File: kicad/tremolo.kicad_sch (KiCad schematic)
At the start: 20 parts, among them IC2 TL072CP

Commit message: Datasheet footprints, floor-plan placement, headless autoroute (144/145, DRC 0)
PCB-AUDIT s1 fixes with datasheet-derived project footprints:
- TO-220-5_Vertical_P1.70mm_LM1875 (TI NDH0005D): 1.45 mm pads on the 1.1 mm
  drill -> 0.175 mm annular (was 0.0875, 5 DRC errors); pad-local 0.2 mm clearance
- Bridge_KBP_P3.81mm (Diodes DS39310 KBP404G-KBP410G, pins + ~ ~ -); bridge
  symbol renumbered to the physical order; errata #3 updated (KBU needs a swap)
- value-aware CP/R sizing (real can sizes for 4700/2200/1000 uF, 5 W / 1 W
  resistors, fat pads on the 0R speaker return); Part 4 wire pads for all
  off-board wiring (2.0 mm/1.2 mm signal, 3.0 mm/1.5 mm speaker + transformer)
- VRAW/AC1/AC2 moved into the HighCurrent net class (errata #11)

gen_pcb.py now places to the Part 5 floor plan: balanced columns (Input/Preamp
with Tone stacked below | Reverb/Trem/MRB | Power Amp | PSU), signal order inside
zones with serpentine shelves, LM1875/LM317 on the top edge with the 10 mm
keep-out, wiring edge along the bottom, 4x M3 holes, two locked 0.9 mm escape
stubs off the LM1875 pins 4/5 (a 1.5/2.5 mm trace cannot enter a 1.70 mm pitch).
DRC before routing: 0 errors, 0 warnings.

route_board.py: pcbnew DSN export -> Freerouting -> SES import -> pour refill.
Freerouting 2.1.0 ignores every pass/timeout limit in CLI mode and only writes
output at 0 unrouted (and its MT router crashed), so the script drives 1.9.0
under xvfb-run and injects autoroute_settings (bottom layer 6x cost, via 80) so
the GND pour stays whole. Committed board: 144/145 connections routed, 0 DRC
violations (--severity-all), 26 vias, 351 mm on the bottom vs 3.7 m on top; the
one open PA_OUT link (blocked by R_bias1) is documented as a GUI finish.

Chassis-fit figure corrected: the old 48-53 % / 82-90 % densities counted hidden
text boxes; text-less it is ~33 % on 190x115 and ~56 % on 155x90.

Docs: PCB-NOTES/PCB-AUDIT rewritten, README, CHANGELOG, errata #3/#11,
SOURCES (package drawings), Part 10, kicad RE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
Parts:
- C_dc_blk: footprint Capacitor_THT:CP_Radial_D8.0mm_P3.50mm -> Capacitor_THT:CP_Radial_D5.0mm_P2.00mm
- POT_DPT, POT_SPD: footprint Connector_PinHeader_2.54mm:PinHeader_1x03_P2.54mm_Vertical -> cambridge_reverb:WirePad_1x03_P2.54mm_D1.2mm
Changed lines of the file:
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@@
     (pin "8")
     (pin "4")
-    (instances (project "cambridge_reverb" (path "/d42230cc-952b-4e7b-8b81-b7cfcd0de5be" (reference "IC2") (unit 1))))
+    (instances (project "cambridge_reverb" (path "/22b2c6fc-b800-4b3c-8b0c-9c9dd16d6c3e" (reference "IC2") (unit 1))))
   )
   (wire (pts (xy 191.76999999999998 116.84) (xy 189.23 116.84)) (stroke (width 0) (type default)))
@@
     (pin "1")
     (pin "2")
-    (instances (project "cambridge_reverb" (path "/d42230cc-952b-4e7b-8b81-b7cfcd0de5be" (reference "C_obuf_in") (unit 1))))
+    (instances (project "cambridge_reverb" (path "/22b2c6fc-b800-4b3c-8b0c-9c9dd16d6c3e" (reference "C_obuf_in") (unit 1))))
   )
   (wire (pts (xy 119.38 71.12) (xy 116.84 71.12)) (stroke (width 0) (type default)))
@@
     (pin "1")
     (pin "2")
-    (instances (project "cambridge_reverb" (path "/d42230cc-952b-4e7b-8b81-b7cfcd0de5be" (reference "R_obuf_b") (unit 1))))
+    (instances (project "cambridge_reverb" (path "/22b2c6fc-b800-4b3c-8b0c-9c9dd16d6c3e" (reference "R_obuf_b") (unit 1))))
   )
   (wire (pts (xy 119.38 101.6) (xy 116.84 101.6)) (stroke (width 0) (type default)))
@@
     (pin "1")
     (pin "2")
-    (instances (project "cambridge_reverb" (path "/d42230cc-952b-4e7b-8b81-b7cfcd0de5be" (reference "R_lfo_ser") (unit 1))))
+    (instances (project "cambridge_reverb" (path "/22b2c6fc-b800-4b3c-8b0c-9c9dd16d6c3e" (reference "R_lfo_ser") (unit 1))))
   )
   (wire (pts (xy 228.59999999999997 86.36) (xy 226.06 86.36)) (stroke (width 0) (type default)))
@@
     (property "Reference" "POT_SPD" (at 266.70000000000005 78.74 0) (effects (font (size 1.27 1.27)) (justify left)))
     (property "Value" "500k lin" (at 266.70000000000005 81.28 0) (effects (font (size 1.27 1.27)) (justify left)))
-    (property "Footprint" "Connector_PinHeader_2.54mm:PinHeader_1x03_P2.54mm_Vertical" (at 264.16 86.36 0) (effects (font (size 1.27 1.27)) hide))
+    (property "Footprint" "cambridge_reverb:WirePad_1x03_P2.54mm_D1.2mm" (at 264.16 86.36 0) (effects (font (size 1.27 1.27)) hide))
     (pin "1")
     (pin "3")
     (pin "2")
-    (instances (project "cambridge_reverb" (path "/d42230cc-952b-4e7b-8b81-b7cfcd0de5be" (reference "POT_SPD") (unit 1))))
+    (instances (project "cambridge_reverb" (path "/22b2c6fc-b800-4b3c-8b0c-9c9dd16d6c3e" (reference "POT_SPD") (unit 1))))
   )
   (wire (pts (xy 259.08 86.36) (xy 256.54 86.36)) (stroke (width 0) (type default)))
@@
     (pin "1")
     (pin "2")
-    (instances (project "cambridge_reverb" (path "/d42230cc-952b-4e7b-8b81-b7cfcd0de5be" (reference "C_lfo1") (unit 1))))
+    (instances (project "cambridge_reverb" (path "/22b2c6fc-b800-4b3c-8b0c-9c9dd16d6c3e" (reference "C_lfo1") (unit 1))))
   )
   (wire (pts (xy 288.28999999999996 91.44) (xy 285.75 91.44)) (stroke (width 0) (type default)))
@@
     (pin "1")
     (pin "2")
-    (instances (project "cambridge_reverb" (path "/d42230cc-952b-4e7b-8b81-b7cfcd0de5be" (reference "R_lfo1") (unit 1))))
+    (instances (project "cambridge_reverb" (path "/22b2c6fc-b800-4b3c-8b0c-9c9dd16d6c3e" (reference "R_lfo1") (unit 1))))
   )
   (wire (pts (xy 238.76 151.13) (xy 236.22000000000003 151.13)) (stroke (width 0) (type default)))
@@
     (pin "1")
     (pin "2")
-    (instances (project "cambridge_reverb" (path "/d42230cc-952b-4e7b-8b81-b7cfcd0de5be" (reference "C_lfo2") (unit 1))))
+    (instances (project "cambridge_reverb" (path "/22b2c6fc-b800-4b3c-8b0c-9c9dd16d6c3e" (reference "C_lfo2") (unit 1))))
   )
   (wire (pts (xy 274.32 151.13) (xy 271.78 151.13)) (stroke (width 0) (type default)))
@@
     (pin "1")
     (pin "2")
-    (instances (project "cambridge_reverb" (path "/d42230cc-952b-4e7b-8b81-b7cfcd0de5be" (reference "R_lfo_fb1") (unit 1))))
+    (instances (project "cambridge_reverb" (path "/22b2c6fc-b800-4b3c-8b0c-9c9dd16d6c3e" (reference "R_lfo_fb1") (unit 1))))
   )
   (wire (pts (xy 158.75 101.6) (xy 156.21 101.6)) (stroke (width 0) (type default)))
@@
     (pin "1")
     (pin "2")
-    (instances (project "cambridge_reverb" (path "/d42230cc-952b-4e7b-8b81-b7cfcd0de5be" (reference "R_lfo_fb2") (unit 1))))
+    (instances (project "cambridge_reverb" (path "/22b2c6fc-b800-4b3c-8b0c-9c9dd16d6c3e" (reference "R_lfo_fb2") (unit 1))))
   )
   (wire (pts (xy 158.75 142.24) (xy 156.21 142.24)) (stroke (width 0) (type default)))
@@
     (pin "1")
     (pin "2")
-    (instances (project "cambridge_reverb" (path "/d42230cc-952b-4e7b-8b81-b7cfcd0de5be" (reference "D_lfo1") (unit 1))))
+    (instances (project "cambridge_reverb" (path "/22b2c6fc-b800-4b3c-8b0c-9c9dd16d6c3e" (reference "D_lfo1") (unit 1))))
   )
   (wire (pts (xy 128.27 101.6) (xy 125.73 101.6)) (stroke (width 0) (type default)))
@@
     (pin "1")
     (pin "2")
-    (instances (project "cambridge_reverb" (path "/d42230cc-952b-4e7b-8b81-b7cfcd0de5be" (reference "D_lfo2") (unit 1))))
+    (instances (project "cambridge_reverb" (path "/22b2c6fc-b800-4b3c-8b0c-9c9dd16d6c3e" (reference "D_lfo2") (unit 1))))
   )
   (wire (pts (xy 128.27 132.07999999999998) (xy 125.73 132.07999999999998)) (stroke (width 0) (type default)))
@@
     (property "Reference" "POT_DPT" (at 212.09 173.99 0) (effects (font (size 1.27 1.27)) (justify left)))
     (property "Value" "100k lin" (at 212.09 176.53 0) (effects (font (size 1.27 1.27)) (justify left)))
-    (property "Footprint" "Connector_PinHeader_2.54mm:PinHeader_1x03_P2.54mm_Vertical" (at 209.55 181.61 0) (effects (font (size 1.27 1.27)) hide))
+    (property "Footprint" "cambridge_reverb:WirePad_1x03_P2.54mm_D1.2mm" (at 209.55 181.61 0) (effects (font (size 1.27 1.27)) hide))
     (pin "1")
     (pin "3")
     (pin "2")
-    (instances (project "cambridge_reverb" (path "/d42230cc-952b-4e7b-8b81-b7cfcd0de5be" (reference "POT_DPT") (unit 1))))
+    (instances (project "cambridge_reverb" (path "/22b2c6fc-b800-4b3c-8b0c-9c9dd16d6c3e" (reference "POT_DPT") (unit 1))))
   )
   (wire (pts (xy 204.47 181.61) (xy 201.93 181.61)) (stroke (width 0) (type default)))
@@
     (pin "1")
     (pin "2")
-    (instances (project "cambridge_reverb" (path "/d42230cc-952b-4e7b-8b81-b7cfcd0de5be" (reference "R_led") (unit 1))))
+    (instances (project "cambridge_reverb" (path "/22b2c6fc-b800-4b3c-8b0c-9c9dd16d6c3e" (reference "R_led") (unit 1))))
   )
   (wire (pts (xy 243.83999999999997 181.61) (xy 241.3 181.61)) (stroke (width 0) (type default)))
@@
     (pin "3")
     (pin "4")
-    (instances (project "cambridge_reverb" (path "/d42230cc-952b-4e7b-8b81-b7cfcd0de5be" (reference "VTL1") (unit 1))))
+    (instances (project "cambridge_reverb" (path "/22b2c6fc-b800-4b3c-8b0c-9c9dd16d6c3e" (reference "VTL1") (unit 1))))
   )
   (wire (pts (xy 285.75 179.07000000000002) (xy 283.21 179.07000000000002)) (stroke (width 0) (type default)))
@@
     (pin "1")
     (pin "2")
-    (instances (project "cambridge_reverb" (path "/d42230cc-952b-4e7b-8b81-b7cfcd0de5be" (reference "R_led_diag") (unit 1))))
+    (instances (project "cambridge_reverb" (path "/22b2c6fc-b800-4b3c-8b0c-9c9dd16d6c3e" (reference "R_led_diag") (unit 1))))
   )
   (wire (pts (xy 238.76 212.09) (xy 236.22000000000003 212.09)) (stroke (width 0) (type default)))
@@
     (pin "1")
     (pin "2")
-    (instances (project "cambridge_reverb" (path "/d42230cc-952b-4e7b-8b81-b7cfcd0de5be" (reference "LED_rate") (unit 1))))
+    (instances (project "cambridge_reverb" (path "/22b2c6fc-b800-4b3c-8b0c-9c9dd16d6c3e" (reference "LED_rate") (unit 1))))
   )
   (wire (pts (xy 284.48 212.09) (xy 281.94 212.09)) (stroke (width 0) (type default)))
@@
     (pin "1")
     (pin "2")
-    (instances (project "cambridge_reverb" (path "/d42230cc-952b-4e7b-8b81-b7cfcd0de5be" (reference "R_trem1") (unit 1))))
+    (instances (project "cambridge_reverb" (path "/22b2c6fc-b800-4b3c-8b0c-9c9dd16d6c3e" (reference "R_trem1") (unit 1))))
   )
   (wire (pts (xy 148.59 181.61) (xy 146.05 181.61)) (stroke (width 0) (type default)))
@@
     (property "Reference" "C_dc_blk" (at 156.21 204.47 0) (effects (font (size 1.27 1.27)) (justify left)))
     (property "Value" "10uF" (at 156.21 207.01 0) (effects (font (size 1.27 1.27)) (justify left)))
-    (property "Footprint" "Capacitor_THT:CP_Radial_D8.0mm_P3.50mm" (at 153.67000000000002 212.09 0) (effects (font (size 1.27 1.27)) hide))
-    (pin "1")
-    (pin "2")
-    (instances (project "cambridge_reverb" (path "/d42230cc-952b-4e7b-8b81-b7cfcd0de5be" (reference "C_dc_blk") (unit 1))))
+    (property "Footprint" "Capacitor_THT:CP_Radial_D5.0mm_P2.00mm" (at 153.67000000000002 212.09 0) (effects (font (size 1.27 1.27)) hide))
+    (pin "1")
+    (pin "2")
+    (instances (project "cambridge_reverb" (path "/22b2c6fc-b800-4b3c-8b0c-9c9dd16d6c3e" (reference "C_dc_blk") (unit 1))))
   )
   (wire (pts (xy 148.59 212.09) (xy 146.05 212.09)) (stroke (width 0) (type default)))
@@
     (pin "1")
     (pin "2")
-    (instances (project "cambridge_reverb" (path "/d42230cc-952b-4e7b-8b81-b7cfcd0de5be" (reference "R_fs_trem") (unit 1))))
+    (instances (project "cambridge_reverb" (path "/22b2c6fc-b800-4b3c-8b0c-9c9dd16d6c3e" (reference "R_fs_trem") (unit 1))))
   )
   (wire (pts (xy 119.38 212.09) (xy 116.84 212.09)) (stroke (width 0) (type default)))

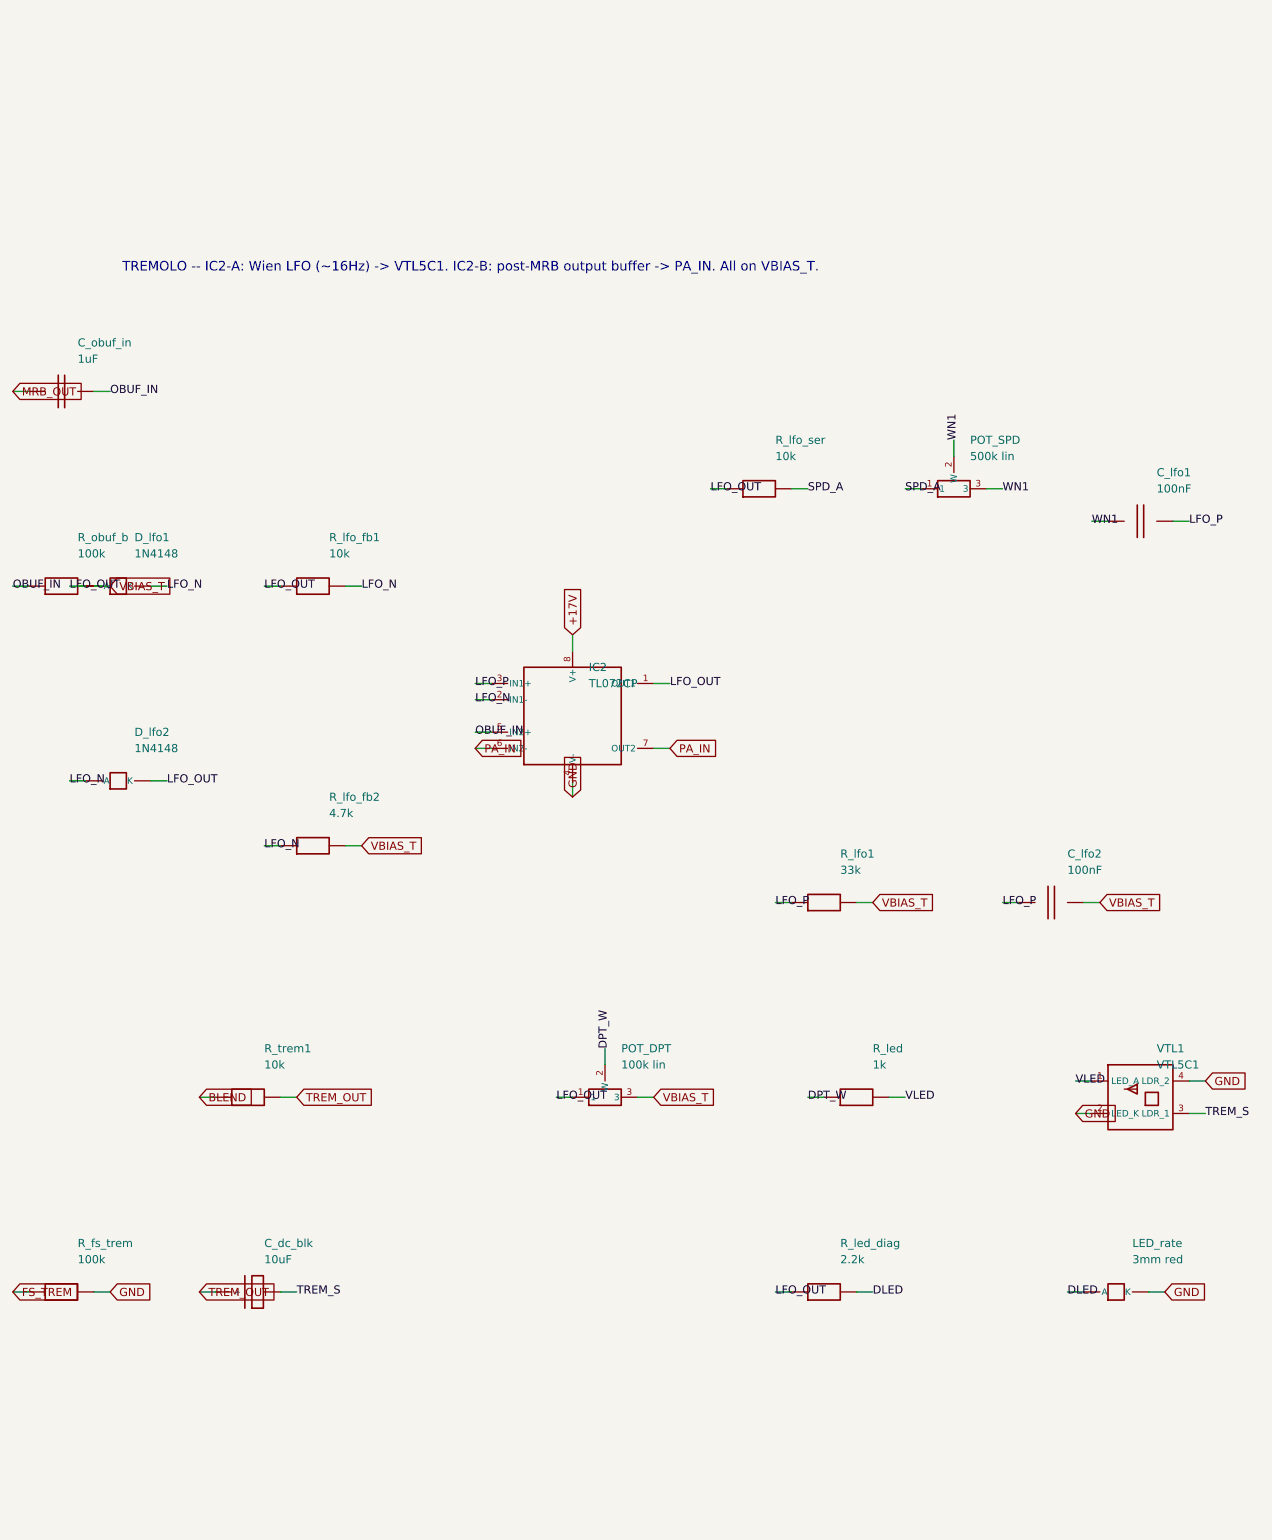
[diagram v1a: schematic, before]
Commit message: Add 26 labelled bench test points (schematic + BOM + silk) and re-route
Test points follow the Part 5 bring-up order: rails (VRAW, +33V5, VREG_IN,
+17V), JFET drains Q1D/Q2D/QRD (the errata #15 bias trim), the VBIAS_R/VBIAS_T
mid-rail refs, every inter-stage node (PREAMP_OUT, TONE_OUT, BLEND, TREM_OUT,
MRB_OUT, PA_IN), tank drive/return, LFO, PA_BIAS/PA_OUT/SPK_P, and a GND pin
per zone for the probe clip.

- gen_kicad.py: one-pin TP symbol; TEST_POINTS table; add_test_points() puts
  them on their sheets so they are in the netlist and the BOM (one order line)
- footprint TestPoint_THT_D2.0mm_Label: 2.0 mm pad / 1.0 mm drill for a header
  pin or wire loop; the footprint VALUE (= net alias) prints on F.SilkS
- gen_pcb.py: test-point strip across the top of each zone; the effects column
  is now two stacked zones (tremolo+MRB above, reverb below next to its tank
  pads) so each block's points sit right above its parts; stacked-zone gap 2 mm
- PCB-NOTES.md: test-point table with expected values (Part 3 troubleshooting,
  Part 2 set-up, ngspice) and the bring-up sequence
- Re-routed (Freerouting 1.9.0, B.Cu x7, via 60): 161/166 connections, 0 DRC
  violations, 54 vias; the five open links are listed for a GUI finish

Co-Authored-By: Claude Fable 5.1 <noreply@anthropic.com>
Claude-Session: https://claude.ai/code/session_01Vk8HkvCugxFpQsBPVnNT2H
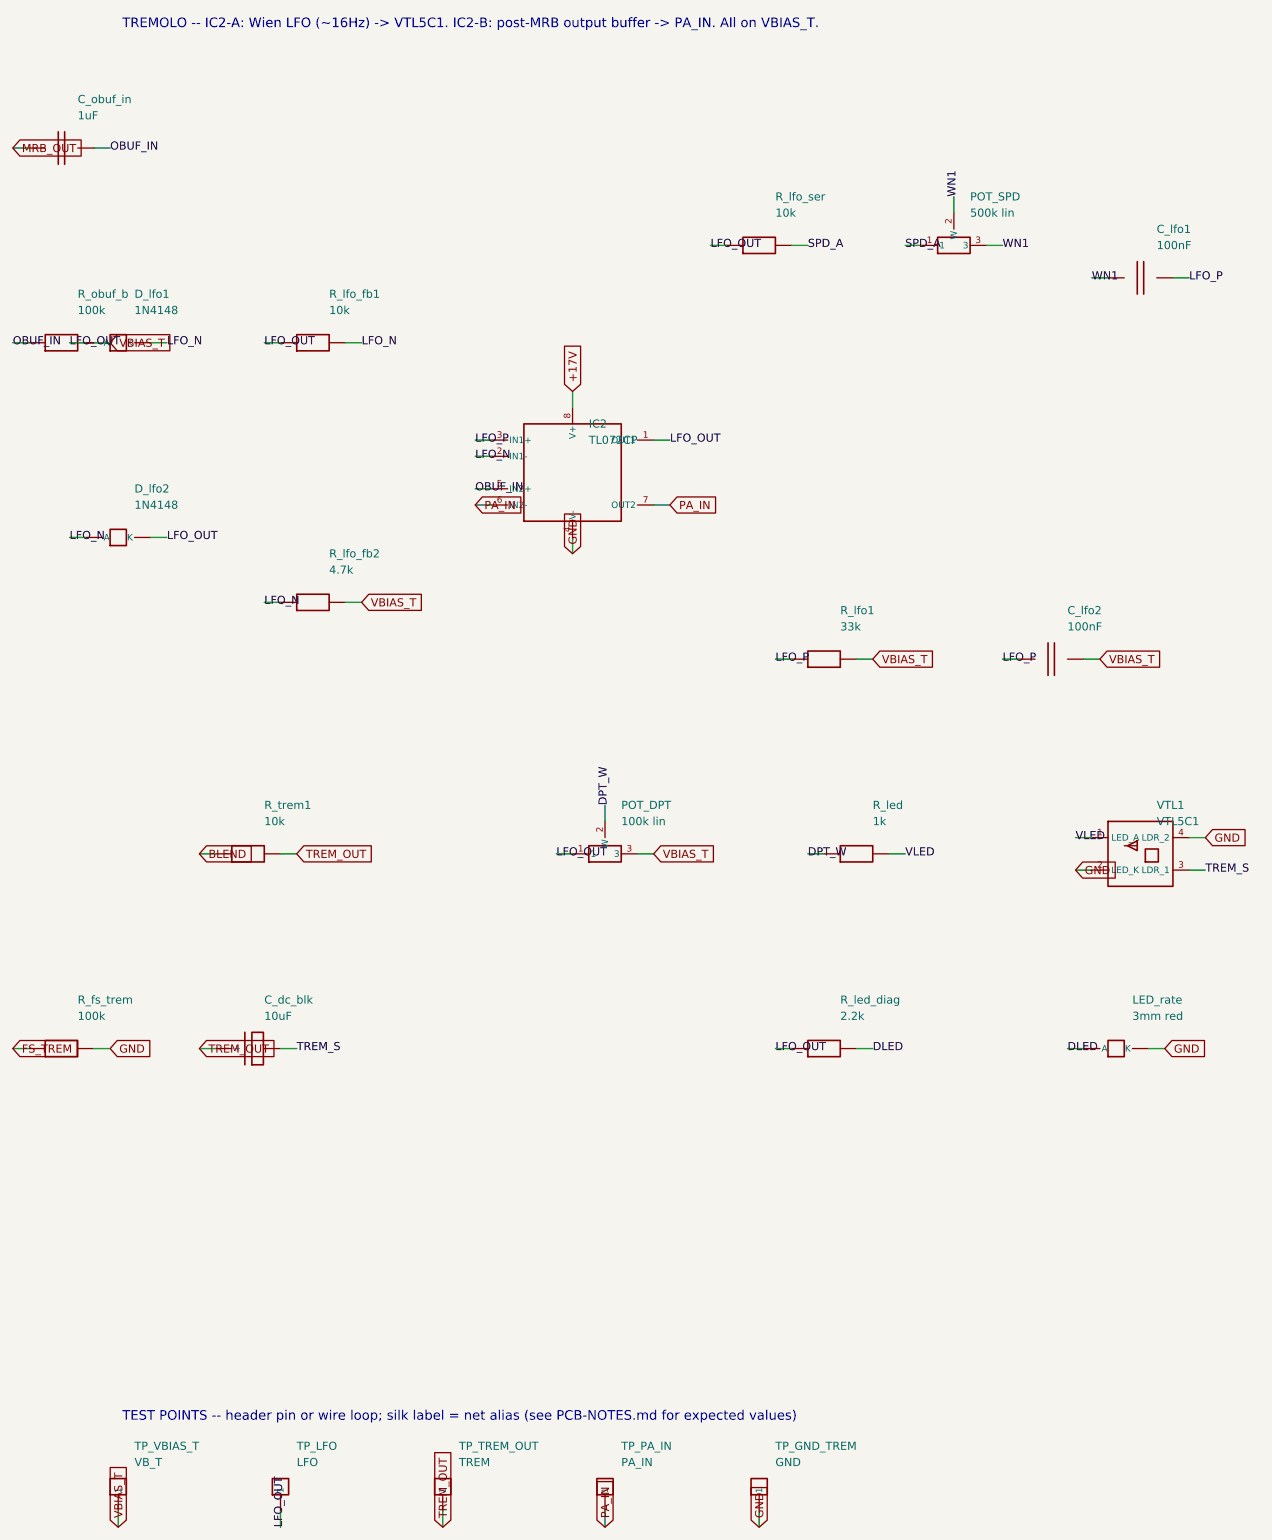
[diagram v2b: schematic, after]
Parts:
- added TP_GND_TREM: GND, cambridge_reverb:TestPoint_THT_D2.0mm_Label, symbol cr_primitives:TP
- added TP_LFO: LFO, cambridge_reverb:TestPoint_THT_D2.0mm_Label, symbol cr_primitives:TP
- added TP_PA_IN: PA_IN, cambridge_reverb:TestPoint_THT_D2.0mm_Label, symbol cr_primitives:TP
- added TP_TREM_OUT: TREM, cambridge_reverb:TestPoint_THT_D2.0mm_Label, symbol cr_primitives:TP
- added TP_VBIAS_T: VB_T, cambridge_reverb:TestPoint_THT_D2.0mm_Label, symbol cr_primitives:TP
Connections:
- net GND: now also TP_GND_TREM.1
- net LFO_OUT: now also TP_LFO.1
- net PA_IN: now also TP_PA_IN.1
- net TREM_OUT: now also TP_TREM_OUT.1
- net VBIAS_T: now also TP_VBIAS_T.1
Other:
- note added: "TEST POINTS -- header pin or wire loop; silk label = net alias (see PCB-NOTES.md for expected values)"
